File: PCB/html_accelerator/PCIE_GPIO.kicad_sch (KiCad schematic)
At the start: 31 parts, among them U1 MCS9990, U3 CAT24C256YI-GT3, Y1 12MHz

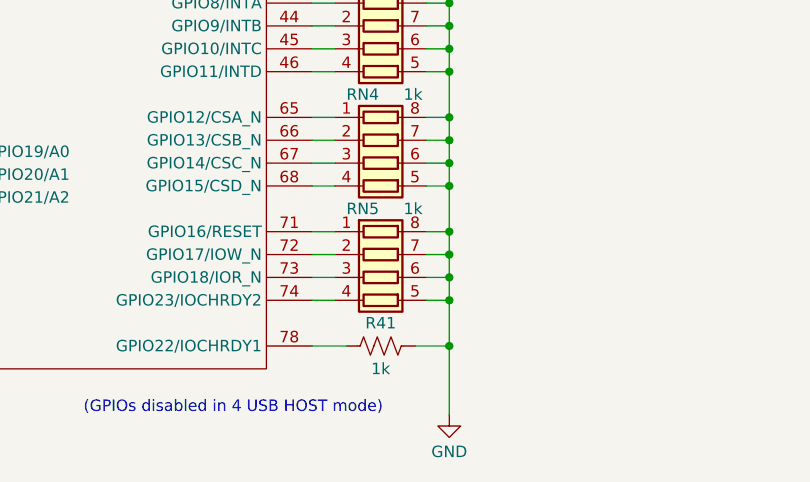
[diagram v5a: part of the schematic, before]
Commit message: Additional routing greebles, cleanup and gerber export with BOM
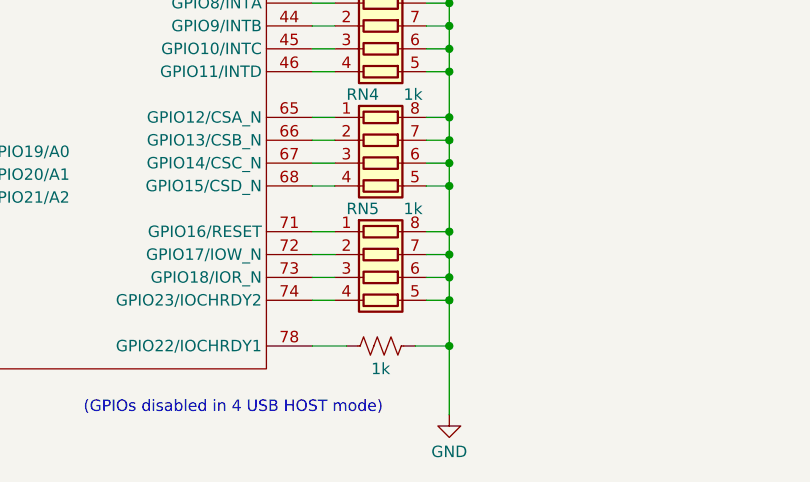
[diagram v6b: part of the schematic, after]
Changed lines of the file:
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@@
 	)
 	(junction
-		(at 134.62 127)
+		(at 134.62 170.18)
 		(diameter 0)
 		(color 0 0 0 0)
 	)
 	(junction
-		(at 69.85 31.75)
+		(at 134.62 127)
 		(diameter 0)
 		(color 0 0 0 0)
 	)
 	(junction
-		(at 134.62 170.18)
+		(at 69.85 31.75)
 		(diameter 0)
 		(color 0 0 0 0)
@@
 	)
 	(junction
+		(at 134.62 165.1)
+		(diameter 0)
+		(color 0 0 0 0)
+	)
+	(junction
 		(at 67.31 123.19)
 		(diameter 0)
@@
 	)
 	(junction
-		(at 110.49 31.75)
+		(at 134.62 162.56)
 		(diameter 0)
 		(color 0 0 0 0)
 	)
 	(junction
-		(at 134.62 157.48)
+		(at 110.49 31.75)
 		(diameter 0)
 		(color 0 0 0 0)
 	)
 	(junction
-		(at 35.56 41.91)
+		(at 134.62 157.48)
 		(diameter 0)
 		(color 0 0 0 0)
 	)
 	(junction
-		(at 134.62 162.56)
+		(at 35.56 41.91)
 		(diameter 0)
 		(color 0 0 0 0)
@@
 	)
 	(junction
-		(at 134.62 165.1)
+		(at 134.62 167.64)
 		(diameter 0)
 		(color 0 0 0 0)
@@
 	)
 	(junction
-		(at 134.62 167.64)
-		(diameter 0)
-		(color 0 0 0 0)
-	)
-	(junction
 		(at 53.34 173.99)
 		(diameter 0)
@@
 	(wire
 		(pts
-			(xy 134.62 165.1) (xy 134.62 167.64)
-		)
-		(stroke
-			(width 0)
-			(type default)
-		)
-	)
-	(wire
-		(pts
 			(xy 123.19 90.17) (xy 123.19 92.71)
 		)
@@
 	(wire
 		(pts
-			(xy 134.62 162.56) (xy 134.62 165.1)
-		)
-		(stroke
-			(width 0)
-			(type default)
-		)
-	)
-	(wire
-		(pts
-			(xy 134.62 167.64) (xy 132.08 167.64)
-		)
-		(stroke
-			(width 0)
-			(type default)
-		)
-	)
-	(wire
-		(pts
 			(xy 134.62 116.84) (xy 132.08 116.84)
 		)
@@
 	(wire
 		(pts
-			(xy 134.62 165.1) (xy 132.08 165.1)
-		)
-		(stroke
-			(width 0)
-			(type default)
-		)
-	)
-	(wire
-		(pts
 			(xy 134.62 142.24) (xy 132.08 142.24)
 		)
@@
 	(wire
 		(pts
-			(xy 121.92 170.18) (xy 119.38 170.18)
-		)
-		(stroke
-			(width 0)
-			(type default)
-		)
-	)
-	(wire
-		(pts
 			(xy 41.91 25.4) (xy 40.64 25.4)
 		)
@@
 	(wire
 		(pts
-			(xy 134.62 167.64) (xy 134.62 170.18)
-		)
-		(stroke
-			(width 0)
-			(type default)
-		)
-	)
-	(wire
-		(pts
 			(xy 64.77 156.21) (xy 77.47 156.21)
 		)
@@
 	(wire
 		(pts
-			(xy 134.62 170.18) (xy 132.08 170.18)
+			(xy 134.62 165.1) (xy 134.62 167.64)
 		)
 		(stroke
@@
 	(wire
 		(pts
-			(xy 134.62 170.18) (xy 134.62 175.26)
+			(xy 52.07 114.3) (xy 77.47 114.3)
 		)
 		(stroke
@@
 	(wire
 		(pts
-			(xy 52.07 114.3) (xy 77.47 114.3)
+			(xy 132.08 162.56) (xy 134.62 162.56)
 		)
 		(stroke
@@
 	(wire
 		(pts
+			(xy 121.92 162.56) (xy 119.38 162.56)
+		)
+		(stroke
+			(width 0)
+			(type default)
+		)
+	)
+	(wire
+		(pts
 			(xy 140.97 92.71) (xy 193.04 92.71)
 		)
@@
 	(wire
 		(pts
-			(xy 72.39 158.75) (xy 77.47 158.75)
+			(xy 121.92 167.64) (xy 119.38 167.64)
 		)
 		(stroke
@@
 	(wire
 		(pts
-			(xy 115.57 90.17) (xy 115.57 92.71)
+			(xy 72.39 158.75) (xy 77.47 158.75)
 		)
 		(stroke
@@
 	(wire
 		(pts
-			(xy 134.62 162.56) (xy 132.08 162.56)
+			(xy 115.57 90.17) (xy 115.57 92.71)
 		)
 		(stroke
@@
 	(wire
 		(pts
+			(xy 134.62 170.18) (xy 134.62 175.26)
+		)
+		(stroke
+			(width 0)
+			(type default)
+		)
+	)
+	(wire
+		(pts
 			(xy 59.69 137.16) (xy 52.07 137.16)
 		)
@@
 	(wire
 		(pts
-			(xy 67.31 116.84) (xy 77.47 116.84)
+			(xy 132.08 167.64) (xy 134.62 167.64)
 		)
 		(stroke
@@
 	(wire
 		(pts
-			(xy 133.35 78.74) (xy 147.32 78.74)
+			(xy 67.31 116.84) (xy 77.47 116.84)
 		)
 		(stroke
@@
 	(wire
 		(pts
-			(xy 24.13 60.96) (xy 24.13 73.66)
+			(xy 133.35 78.74) (xy 147.32 78.74)
 		)
 		(stroke
@@
 	(wire
 		(pts
-			(xy 121.92 111.76) (xy 119.38 111.76)
+			(xy 121.92 165.1) (xy 119.38 165.1)
 		)
 		(stroke
@@
 	(wire
 		(pts
-			(xy 38.1 66.04) (xy 41.91 66.04)
+			(xy 24.13 60.96) (xy 24.13 73.66)
 		)
 		(stroke
@@
 	(wire
 		(pts
-			(xy 24.13 58.42) (xy 41.91 58.42)
+			(xy 121.92 111.76) (xy 119.38 111.76)
 		)
 		(stroke
@@
 	(wire
 		(pts
-			(xy 59.69 138.43) (xy 59.69 137.16)
+			(xy 38.1 66.04) (xy 41.91 66.04)
 		)
 		(stroke
@@
 	(wire
 		(pts
-			(xy 121.92 167.64) (xy 119.38 167.64)
+			(xy 24.13 58.42) (xy 41.91 58.42)
 		)
 		(stroke
@@
 	(wire
 		(pts
-			(xy 69.85 60.96) (xy 147.32 60.96)
+			(xy 59.69 138.43) (xy 59.69 137.16)
 		)
 		(stroke
@@
 	(wire
 		(pts
-			(xy 121.92 162.56) (xy 119.38 162.56)
+			(xy 69.85 60.96) (xy 147.32 60.96)
 		)
 		(stroke
@@
 	(wire
 		(pts
+			(xy 134.62 167.64) (xy 134.62 170.18)
+		)
+		(stroke
+			(width 0)
+			(type default)
+		)
+	)
+	(wire
+		(pts
+			(xy 121.92 170.18) (xy 119.38 170.18)
+		)
+		(stroke
+			(width 0)
+			(type default)
+		)
+	)
+	(wire
+		(pts
 			(xy 134.62 119.38) (xy 134.62 124.46)
 		)
@@
 	(wire
 		(pts
+			(xy 132.08 170.18) (xy 134.62 170.18)
+		)
+		(stroke
+			(width 0)
+			(type default)
+		)
+	)
+	(wire
+		(pts
+			(xy 134.62 162.56) (xy 134.62 165.1)
+		)
+		(stroke
+			(width 0)
+			(type default)
+		)
+	)
+	(wire
+		(pts
 			(xy 30.48 63.5) (xy 41.91 63.5)
 		)
@@
 	(wire
 		(pts
-			(xy 134.62 149.86) (xy 134.62 152.4)
+			(xy 132.08 165.1) (xy 134.62 165.1)
 		)
 		(stroke
@@
 	(wire
 		(pts
-			(xy 24.13 87.63) (xy 30.48 87.63)
+			(xy 134.62 149.86) (xy 134.62 152.4)
 		)
 		(stroke
@@
 	(wire
 		(pts
-			(xy 137.16 45.72) (xy 147.32 45.72)
+			(xy 24.13 87.63) (xy 30.48 87.63)
 		)
 		(stroke
@@
 	(wire
 		(pts
-			(xy 134.62 124.46) (xy 132.08 124.46)
+			(xy 137.16 45.72) (xy 147.32 45.72)
 		)
 		(stroke
@@
 	(wire
 		(pts
-			(xy 134.62 137.16) (xy 132.08 137.16)
+			(xy 134.62 124.46) (xy 132.08 124.46)
 		)
 		(stroke
@@
 	(wire
 		(pts
-			(xy 134.62 127) (xy 132.08 127)
+			(xy 134.62 137.16) (xy 132.08 137.16)
 		)
 		(stroke
@@
 	(wire
 		(pts
-			(xy 121.92 165.1) (xy 119.38 165.1)
+			(xy 134.62 127) (xy 132.08 127)
 		)
 		(stroke
@@
 			)
 		)
-		(property "Description" ""
+		(property "Description" "4 resistor network, parallel topology"
 			(at 127 129.54 0)
+			(hide yes)
 			(show_name no)
 			(do_not_autoplace no)
@@
 			)
 		)
-		(property "Description" ""
+		(property "Description" "4 resistor network, parallel topology"
 			(at 127 116.84 0)
+			(hide yes)
 			(show_name no)
 			(do_not_autoplace no)
@@
 			)
 		)
-		(property "Description" ""
+		(property "Description" "4 resistor network, parallel topology"
 			(at 127 142.24 0)
+			(hide yes)
 			(show_name no)
 			(do_not_autoplace no)
@@
 			)
 		)
-		(property "Description" ""
+		(property "Description" "4 resistor network, parallel topology"
 			(at 127 154.94 0)
+			(hide yes)
 			(show_name no)
 			(do_not_autoplace no)
@@
 		(property "Reference" "R41"
 			(at 127 172.72 90)
+			(hide yes)
 			(show_name no)
 			(do_not_autoplace no)
@@
 	)
 	(symbol
+		(lib_name "R_Pack04_1")
 		(lib_id "Device:R_Pack04")
 		(at 127 167.64 270)
@@
 			)
 		)
-		(property "Description" ""
+		(property "Description" "4 resistor network, parallel topology"
 			(at 127 167.64 0)
+			(hide yes)
 			(show_name no)
 			(do_not_autoplace no)

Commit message: gerbers and readme updates
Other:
- company: (none) -> Spencer K
- title: EEPROM, CFG, GPIO -> HTML Accelerator
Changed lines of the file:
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@@
 	(paper "A4")
 	(title_block
-		(title "EEPROM, CFG, GPIO")
-		(date "2024-09-15")
-		(rev "1")
+		(title "HTML Accelerator")
+		(date "2026-04-25")
+		(rev "1.0")
+		(company "Spencer K")
+		(comment 1 "https://github.com/akaStanley/HTML_Accelerator")
 	)
 	(text "A0,A1,A2\nBoostrap Options"

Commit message: updated gerbers for fab
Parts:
- C36, C37: value 22pF -> 20pF
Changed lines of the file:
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@@
 	(title_block
 		(title "HTML Accelerator")
-		(date "2026-04-25")
+		(date "2026-04-29")
 		(rev "1.0")
 		(company "Spencer K")
@@
 			)
 		)
-		(property "Value" "22pF"
+		(property "Value" "20pF"
 			(at 62.23 132.08 0)
 			(show_name no)
@@
 			)
 		)
-		(property "Value" "22pF"
+		(property "Value" "20pF"
 			(at 46.99 132.08 0)
 			(show_name no)
